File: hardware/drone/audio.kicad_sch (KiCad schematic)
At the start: 21 parts, among them J6 Conn_01x02_Socket, U11 TAC5111IRGER, U28 LM4670ITL/NOPB

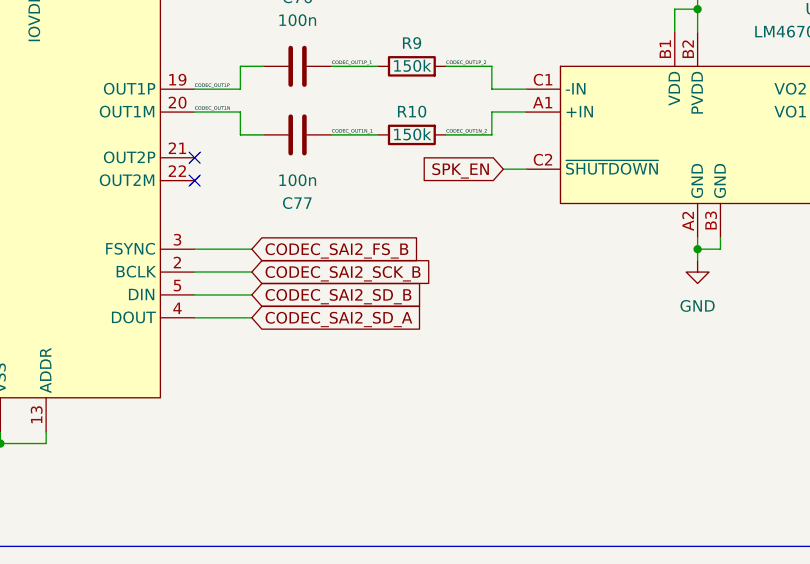
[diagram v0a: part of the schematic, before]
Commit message: Routed SX1262 SPI and placed decaps for codec
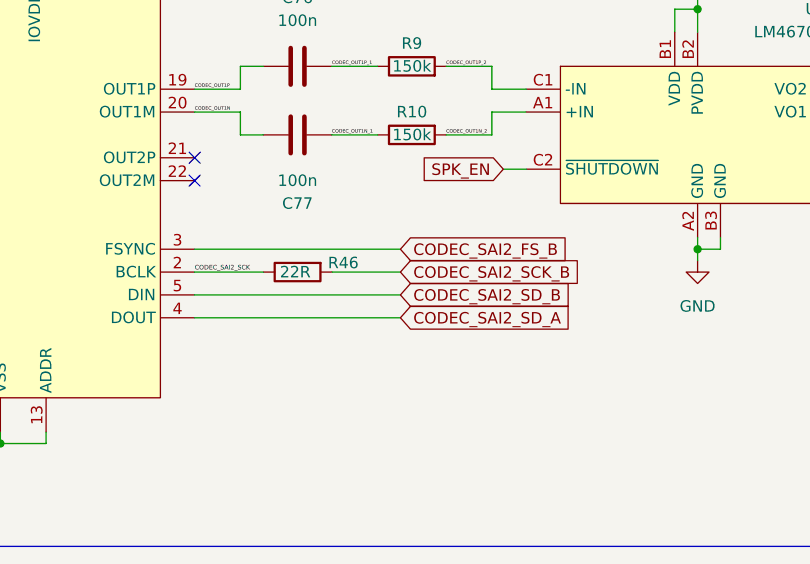
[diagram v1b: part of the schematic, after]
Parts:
- added R46: 22R, Resistor_SMD:R_0201_0603Metric, symbol Device:R
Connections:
- net CODEC_SAI2_SCK_B: now also R46.2; no longer U11.2 (BCLK)
- new net CODEC_SAI2_SCK: R46.1, U11.2 (BCLK)
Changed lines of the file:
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@@
-	(wire
-		(pts
-			(xy 154.94 105.41) (xy 148.59 105.41)
-		)
-		(stroke
-			(width 0)
-			(type default)
-		)
-	)
 	(wire
 		(pts
@@
 	(wire
 		(pts
-			(xy 154.94 102.87) (xy 148.59 102.87)
-		)
-		(stroke
-			(width 0)
-			(type default)
-		)
-	)
-	(wire
-		(pts
 			(xy 220.98 80.01) (xy 227.33 80.01)
 		)
@@
 	(wire
 		(pts
+			(xy 148.59 105.41) (xy 171.45 105.41)
+		)
+		(stroke
+			(width 0)
+			(type default)
+		)
+	)
+	(wire
+		(pts
 			(xy 132.08 119.38) (xy 127 119.38)
 		)
@@
 	(wire
 		(pts
+			(xy 148.59 102.87) (xy 171.45 102.87)
+		)
+		(stroke
+			(width 0)
+			(type default)
+		)
+	)
+	(wire
+		(pts
 			(xy 144.78 33.02) (xy 144.78 34.29)
 		)
@@
 	(wire
 		(pts
-			(xy 154.94 97.79) (xy 148.59 97.79)
-		)
-		(stroke
-			(width 0)
-			(type default)
-		)
-	)
-	(wire
-		(pts
 			(xy 173.99 63.5) (xy 173.99 62.23)
 		)
@@
 	(wire
 		(pts
+			(xy 148.59 100.33) (xy 156.21 100.33)
+		)
+		(stroke
+			(width 0)
+			(type default)
+		)
+	)
+	(wire
+		(pts
 			(xy 49.53 58.42) (xy 49.53 74.93)
 		)
@@
 	(wire
 		(pts
+			(xy 148.59 97.79) (xy 171.45 97.79)
+		)
+		(stroke
+			(width 0)
+			(type default)
+		)
+	)
+	(wire
+		(pts
 			(xy 201.93 73.66) (xy 201.93 71.12)
 		)
@@
 	(wire
 		(pts
-			(xy 154.94 100.33) (xy 148.59 100.33)
-		)
-		(stroke
-			(width 0)
-			(type default)
-		)
-	)
-	(wire
-		(pts
 			(xy 124.46 119.38) (xy 121.92 119.38)
 		)
@@
 	(wire
 		(pts
+			(xy 163.83 100.33) (xy 171.45 100.33)
+		)
+		(stroke
+			(width 0)
+			(type default)
+		)
+	)
+	(wire
+		(pts
 			(xy 125.73 64.77) (xy 125.73 33.02)
 		)
@@
 			(width 0)
 			(type default)
+		)
+	)
+	(label "CODEC_SAI2_SCK"
+		(at 148.59 100.33 0)
+		(effects
+			(font
+				(size 0.508 0.508)
+			)
+			(justify left bottom)
 		)
 	)
@@
 	(global_label "CODEC_SAI2_SD_B"
 		(shape input)
-		(at 154.94 102.87 0)
+		(at 171.45 102.87 0)
 		(fields_autoplaced yes)
 		(effects
@@
 		)
 		(property "Intersheetrefs" "${INTERSHEET_REFS}"
-			(at 174.9794 102.87 0)
+			(at 191.4894 102.87 0)
 			(hide yes)
 			(show_name no)
@@
 	(global_label "CODEC_SAI2_SCK_B"
 		(shape input)
-		(at 154.94 100.33 0)
+		(at 171.45 100.33 0)
 		(fields_autoplaced yes)
 		(effects
@@
 		)
 		(property "Intersheetrefs" "${INTERSHEET_REFS}"
-			(at 174.798 100.33 0)
+			(at 192.7594 100.33 0)
 			(hide yes)
 			(show_name no)
@@
 	(global_label "CODEC_SAI2_FS_B"
 		(shape input)
-		(at 154.94 97.79 0)
+		(at 171.45 97.79 0)
 		(fields_autoplaced yes)
 		(effects
@@
 		)
 		(property "Intersheetrefs" "${INTERSHEET_REFS}"
-			(at 176.2494 97.79 0)
+			(at 192.7594 97.79 0)
 			(hide yes)
 			(show_name no)
@@
 	(global_label "CODEC_SAI2_SD_A"
 		(shape input)
-		(at 154.94 105.41 0)
+		(at 171.45 105.41 0)
 		(fields_autoplaced yes)
 		(effects
@@
 		)
 		(property "Intersheetrefs" "${INTERSHEET_REFS}"
-			(at 174.798 105.41 0)
+			(at 191.308 105.41 0)
 			(hide yes)
 			(show_name no)
@@
 					(unit 1)
 				)
+			)
+		)
+	)
+	(symbol
+		(lib_id "Device:R")
+		(at 160.02 100.33 90)
+		(mirror x)
+		(unit 1)
+		(body_style 1)
+		(exclude_from_sim no)
+		(in_bom yes)
+		(on_board yes)
+		(in_pos_files yes)
+		(dnp no)
+		(property "Reference" "R46"
+			(at 165.1 99.314 90)
+			(show_name no)
+			(do_not_autoplace no)
+			(effects
+				(font
+					(size 1.27 1.27)
+				)
+			)
+		)
+		(property "Value" "22R"
+			(at 159.766 100.33 90)
+			(show_name no)
+			(do_not_autoplace no)
+			(effects
+				(font
+					(size 1.27 1.27)
+				)
+			)
+		)
+		(property "Footprint" "Resistor_SMD:R_0201_0603Metric"
+			(at 160.02 98.552 90)
+			(hide yes)
+			(show_name no)
+			(do_not_autoplace no)
+			(effects
+				(font
+					(size 1.27 1.27)
+				)
+			)
+		)
+		(property "Datasheet" ""
+			(at 160.02 100.33 0)
+			(hide yes)
+			(show_name no)
+			(do_not_autoplace no)
+			(effects
+				(font
+					(size 1.27 1.27)
+				)
+			)
+		)
+		(property "Description" "Resistor"
+			(at 160.02 100.33 0)
+			(hide yes)
+			(show_name no)
+			(do_not_autoplace no)
+			(effects
+				(font
+					(size 1.27 1.27)
+				)
+			)
+		)
+		(pin "2"
+		)
+		(pin "1"
+		)
+		(instances
+			(project "drone"
+				(path "/62c402a6-ed3f-446b-8423-821e9cc6908b/c9707772-454c-4a11-9731-f4c991bbc034"
+					(reference "R46")
+					(unit 1)
+				)

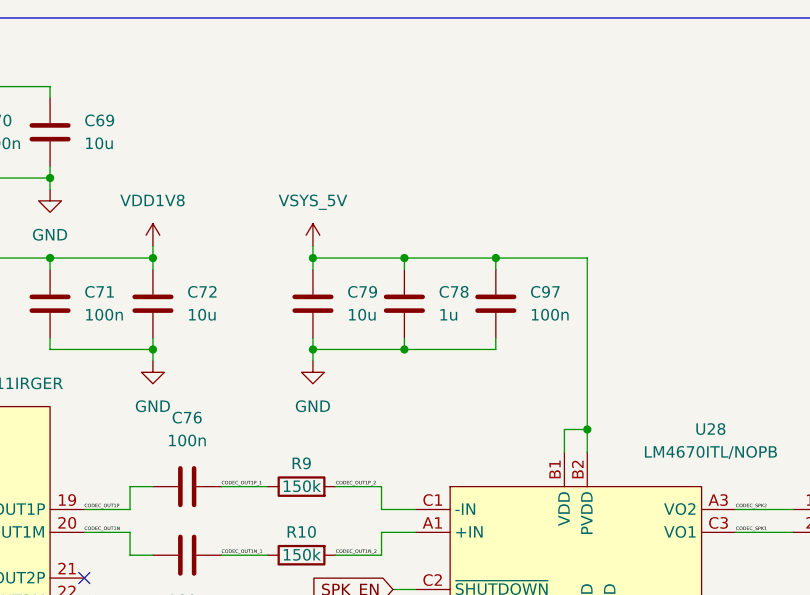
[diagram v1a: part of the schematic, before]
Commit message: More audio routing
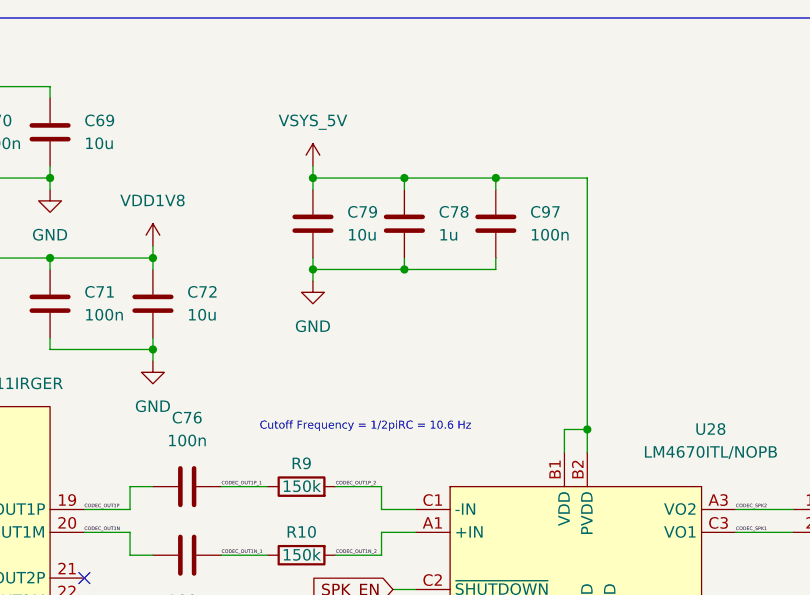
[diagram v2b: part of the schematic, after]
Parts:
- C78, C97: footprint Capacitor_SMD:C_0603_1608Metric -> Capacitor_SMD:C_0402_1005Metric
- R46: footprint Resistor_SMD:R_0201_0603Metric -> Resistor_SMD:R_0402_1005Metric
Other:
- note added: "Cutoff Frequency = 1/2piRC = 10.6 Hz"
- moved on the sheet: C78, C79, C97
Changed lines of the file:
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@@
 		)
 	)
+	(text "Cutoff Frequency = 1/2piRC = 10.6 Hz"
+		(exclude_from_sim no)
+		(at 179.832 70.866 0)
+		(effects
+			(font
+				(size 0.889 0.889)
+			)
+		)
+	)
 	(text "20MM-4Ω3W\nC50387236"
 		(exclude_from_sim no)
@@
 	)
 	(junction
-		(at 184.15 62.23)
+		(at 184.15 53.34)
 		(diameter 0)
 		(color 0 0 0 0)
 	)
 	(junction
-		(at 173.99 62.23)
+		(at 173.99 53.34)
 		(diameter 0)
 		(color 0 0 0 0)
@@
 	)
 	(junction
-		(at 184.15 52.07)
+		(at 184.15 43.18)
 		(diameter 0)
 		(color 0 0 0 0)
@@
 	)
 	(junction
-		(at 194.31 52.07)
+		(at 194.31 43.18)
 		(diameter 0)
 		(color 0 0 0 0)
 	)
 	(junction
-		(at 173.99 52.07)
+		(at 173.99 43.18)
 		(diameter 0)
 		(color 0 0 0 0)
@@
 	(wire
 		(pts
-			(xy 173.99 62.23) (xy 184.15 62.23)
+			(xy 173.99 53.34) (xy 184.15 53.34)
 		)
 		(stroke
@@
 	(wire
 		(pts
-			(xy 184.15 62.23) (xy 184.15 60.96)
+			(xy 184.15 53.34) (xy 184.15 52.07)
 		)
 		(stroke
@@
 	(wire
 		(pts
-			(xy 194.31 60.96) (xy 194.31 62.23)
+			(xy 194.31 52.07) (xy 194.31 53.34)
 		)
 		(stroke
@@
 	(wire
 		(pts
-			(xy 173.99 52.07) (xy 184.15 52.07)
+			(xy 173.99 43.18) (xy 184.15 43.18)
 		)
 		(stroke
@@
 	(wire
 		(pts
-			(xy 194.31 52.07) (xy 194.31 53.34)
+			(xy 194.31 43.18) (xy 194.31 44.45)
 		)
 		(stroke
@@
 	(wire
 		(pts
-			(xy 194.31 62.23) (xy 184.15 62.23)
+			(xy 194.31 53.34) (xy 184.15 53.34)
 		)
 		(stroke
@@
 	(wire
 		(pts
-			(xy 184.15 53.34) (xy 184.15 52.07)
+			(xy 184.15 44.45) (xy 184.15 43.18)
 		)
 		(stroke
@@
 	(wire
 		(pts
-			(xy 173.99 62.23) (xy 173.99 60.96)
+			(xy 173.99 53.34) (xy 173.99 52.07)
 		)
 		(stroke
@@
 	(wire
 		(pts
-			(xy 173.99 53.34) (xy 173.99 52.07)
+			(xy 173.99 44.45) (xy 173.99 43.18)
 		)
 		(stroke
@@
 	(wire
 		(pts
-			(xy 204.47 52.07) (xy 204.47 71.12)
+			(xy 204.47 43.18) (xy 204.47 71.12)
 		)
 		(stroke
@@
 	(wire
 		(pts
-			(xy 173.99 63.5) (xy 173.99 62.23)
+			(xy 173.99 54.61) (xy 173.99 53.34)
 		)
 		(stroke
@@
 	(wire
 		(pts
-			(xy 194.31 52.07) (xy 204.47 52.07)
+			(xy 194.31 43.18) (xy 204.47 43.18)
 		)
 		(stroke
@@
 	(wire
 		(pts
-			(xy 173.99 50.8) (xy 173.99 52.07)
+			(xy 173.99 41.91) (xy 173.99 43.18)
 		)
 		(stroke
@@
 	(wire
 		(pts
-			(xy 184.15 52.07) (xy 194.31 52.07)
+			(xy 184.15 43.18) (xy 194.31 43.18)
 		)
 		(stroke
@@
 	(symbol
 		(lib_id "Device:C")
-		(at 184.15 57.15 0)
+		(at 184.15 48.26 0)
 		(unit 1)
 		(body_style 1)
@@
 		(fields_autoplaced yes)
 		(property "Reference" "C78"
-			(at 187.96 55.8799 0)
+			(at 187.96 46.9899 0)
 			(show_name no)
 			(do_not_autoplace no)
@@
 		)
 		(property "Value" "1u"
-			(at 187.96 58.4199 0)
+			(at 187.96 49.5299 0)
 			(show_name no)
 			(do_not_autoplace no)
@@
 			)
 		)
-		(property "Footprint" "Capacitor_SMD:C_0603_1608Metric"
-			(at 185.1152 60.96 0)
+		(property "Footprint" "Capacitor_SMD:C_0402_1005Metric"
+			(at 185.1152 52.07 0)
 			(hide yes)
 			(show_name no)
@@
 		)
 		(property "Datasheet" ""
-			(at 184.15 57.15 0)
+			(at 184.15 48.26 0)
 			(hide yes)
 			(show_name no)
@@
 		)
 		(property "Description" "Unpolarized capacitor"
-			(at 184.15 57.15 0)
+			(at 184.15 48.26 0)
 			(hide yes)
 			(show_name no)
@@
 	(symbol
 		(lib_id "Device:C")
-		(at 173.99 57.15 0)
+		(at 173.99 48.26 0)
 		(unit 1)
 		(body_style 1)
@@
 		(fields_autoplaced yes)
 		(property "Reference" "C79"
-			(at 177.8 55.8799 0)
+			(at 177.8 46.9899 0)
 			(show_name no)
 			(do_not_autoplace no)
@@
 		)
 		(property "Value" "10u"
-			(at 177.8 58.4199 0)
+			(at 177.8 49.5299 0)
 			(show_name no)
 			(do_not_autoplace no)
@@
 		)
 		(property "Footprint" "Capacitor_SMD:C_0805_2012Metric"
-			(at 174.9552 60.96 0)
+			(at 174.9552 52.07 0)
 			(hide yes)
 			(show_name no)
@@
 		)
 		(property "Datasheet" ""
-			(at 173.99 57.15 0)
+			(at 173.99 48.26 0)
 			(hide yes)
 			(show_name no)
@@
 		)
 		(property "Description" "Unpolarized capacitor"
-			(at 173.99 57.15 0)
+			(at 173.99 48.26 0)
 			(hide yes)
 			(show_name no)
@@
 			)
 		)
-		(property "Footprint" "Resistor_SMD:R_0201_0603Metric"
+		(property "Footprint" "Resistor_SMD:R_0402_1005Metric"
 			(at 160.02 98.552 90)
 			(hide yes)
@@
 	(symbol
 		(lib_id "power:GND")
-		(at 173.99 63.5 0)
+		(at 173.99 54.61 0)
 		(unit 1)
 		(body_style 1)
@@
 		(fields_autoplaced yes)
 		(property "Reference" "#PWR0103"
-			(at 173.99 69.85 0)
+			(at 173.99 60.96 0)
 			(hide yes)
 			(show_name no)
@@
 		)
 		(property "Value" "GND"
-			(at 173.99 68.58 0)
+			(at 173.99 59.69 0)
 			(show_name no)
 			(do_not_autoplace no)
@@
 		)
 		(property "Footprint" ""
-			(at 173.99 63.5 0)
+			(at 173.99 54.61 0)
 			(hide yes)
 			(show_name no)
@@
 		)
 		(property "Datasheet" ""
-			(at 173.99 63.5 0)
+			(at 173.99 54.61 0)
 			(hide yes)
 			(show_name no)
@@
 		)
 		(property "Description" "Power symbol creates a global label with name \"GND\" , ground"
-			(at 173.99 63.5 0)
+			(at 173.99 54.61 0)
 			(hide yes)
 			(show_name no)
@@
 	(symbol
 		(lib_id "Device:C")
-		(at 194.31 57.15 0)
+		(at 194.31 48.26 0)
 		(unit 1)
 		(body_style 1)
@@
 		(fields_autoplaced yes)
 		(property "Reference" "C97"
-			(at 198.12 55.8799 0)
+			(at 198.12 46.9899 0)
 			(show_name no)
 			(do_not_autoplace no)
@@
 		)
 		(property "Value" "100n"
-			(at 198.12 58.4199 0)
+			(at 198.12 49.5299 0)
 			(show_name no)
 			(do_not_autoplace no)
@@
 			)
 		)
-		(property "Footprint" "Capacitor_SMD:C_0603_1608Metric"
-			(at 195.2752 60.96 0)
+		(property "Footprint" "Capacitor_SMD:C_0402_1005Metric"
+			(at 195.2752 52.07 0)
 			(hide yes)
 			(show_name no)
@@
 		)
 		(property "Datasheet" ""
-			(at 194.31 57.15 0)
+			(at 194.31 48.26 0)
 			(hide yes)
 			(show_name no)
@@
 		)
 		(property "Description" "Unpolarized capacitor"
-			(at 194.31 57.15 0)
+			(at 194.31 48.26 0)
 			(hide yes)
 			(show_name no)
@@
 	(symbol
 		(lib_id "power:VDD")
-		(at 173.99 50.8 0)
+		(at 173.99 41.91 0)
 		(unit 1)
 		(body_style 1)
@@
 		(fields_autoplaced yes)
 		(property "Reference" "#PWR0102"
-			(at 173.99 54.61 0)
+			(at 173.99 45.72 0)
 			(hide yes)
 			(show_name no)
@@
 		)
 		(property "Value" "VSYS_5V"
-			(at 173.99 45.72 0)
+			(at 173.99 36.83 0)
 			(show_name no)
 			(do_not_autoplace no)
@@
 		)
 		(property "Footprint" ""
-			(at 173.99 50.8 0)
+			(at 173.99 41.91 0)
 			(hide yes)
 			(show_name no)
@@
 		)
 		(property "Datasheet" ""
-			(at 173.99 50.8 0)
+			(at 173.99 41.91 0)
 			(hide yes)
 			(show_name no)
@@
 		)
 		(property "Description" "Power symbol creates a global label with name \"VDD\""
-			(at 173.99 50.8 0)
+			(at 173.99 41.91 0)
 			(hide yes)
 			(show_name no)
